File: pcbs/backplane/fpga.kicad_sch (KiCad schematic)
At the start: 77 parts, among them J2 Conn_02x15_Odd_Even, J3 Conn_02x20_Odd_Even, Q10 MMBT3906, Q11 MMBT3906, Q9 D44H11G, U10 74LVC2T45, U28 Snickerdoodle, U34 ICS501, U4 PCA9544APW, U5 PCA9544APW, U6 74HC151, U7 AP7361C-25E, U8 74LVC2T45, U9 74LVC2T45

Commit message: Backplane comms updates, manufacturing renaming
Removed misspelled "maunfacturing" folder, fixed gitignore rule to remove manufacturing folders within individual PCB folders too
Changed SCKI/SCKO terminology to SCK, SCK_LB (loopback) for clarity
Added ADC_CS loopback signal between amp ctrl board & backplane for better fast-clock timing (#38)
Backplane: changed LVDS FPGA outputs to single-ended FPGA outputs to gain more I/O pins, added external LVDS transceivers (#38)
Backplane: replaced global clock & ~LDAC buffers with a separate FPGA pin for each amp ctrl board (#38)
Backplane: removed +2.5V power supply and level translations, no longer needed without FPGA I/O pins using LVDS_25 I/O configuration
Backplane: replaced +VDC-input resistor with solder jumper (on by default)
Backplane: changed field names (Part Number to MPN) to match Aisler's naming convention for automatic recognition
Amp ctrl: fixed optional level-shifter circuit on each channel for voltage inputs (#9) schematic & channel-1 layout
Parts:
- removed C25, C27: 1uF 50V X7R, Capacitor_SMD:C_0805_2012Metric, symbol Device:C
- removed C29, C30: 100nF 50V X7R, Capacitor_SMD:C_0603_1608Metric, symbol Device:C
- removed JP34: Jumper_NC_Small, Jumper:SolderJumper-2_P1.3mm_Bridged_RoundedPad1.0x1.5mm, symbol backplane-rescue:Jumper_NC_Small-Device
- removed TP53, TP62: TestPoint, TestPoint:TestPoint_Pad_D2.0mm, symbol Connector:TestPoint
- removed TP7: TestPoint_Flag, TestPoint:TestPoint_Keystone_5019_Miniature, symbol Connector:TestPoint_Flag
- removed U7: AP7361C-25E, Package_TO_SOT_SMD:SOT-223-3_TabPin2, symbol Regulator_Linear:LT1129-3.3_SOT223
- removed U9: 74LVC2T45, Package_SO:VSSOP-8_2.3x2mm_P0.5mm, symbol Logic_LevelTranslator:74LVC2T45DC
- C21, C35: MPN (none) -> C0805C105K3RACTU; Part Number C0805C105K3RACTU -> (none)
- C22, C23, C24, C26, C28, C32, C33, C67: MPN (none) -> C0603C104K5RACTU; Part Number C0603C104K5RACTU -> (none)
- D17: MPN (none) -> UDZVTE-1716B; MPN Alt. (none) -> MM3Z16VB; Part Number UDZVTE-1716B -> (none); Part Number Alt. MM3Z16VB -> (none)
- J2: MPN (none) -> TFM-115-01-S-D-WT; MPN Alt. (none) -> TFM-115-01-L-D-WT, TFM-115-01-F-D-WT; Part Number TFM-115-01-S-D-WT -> (none); Part Number Alt. TFM-115-01-L-D-WT, TFM-115-01-F-D-WT -> (none)
- J3, JA1, JA2, JB1, JB2, JC1: MPN (none) -> TFM-120-01-S-D-WT; MPN Alt. (none) -> TFM-120-01-L-D-WT, TFM-120-01-F-D-WT; Part Number TFM-120-01-S-D-WT -> (none); Part Number Alt. TFM-120-01-L-D-WT, TFM-120-01-F-D-WT -> (none)
- Q10, Q11: MPN (none) -> MMBT3906-7-F; MPN Alt. (none) -> MMBT3906,215; Part Number MMBT3906-7-F -> (none); Part Number Alt. MMBT3906,215 -> (none)
- Q9: MPN (none) -> D44H11G; Part Number D44H11G -> (none)
- R14, R15: MPN (none) -> RK73H2ATTD4701F; Part Number RK73H2ATTD4701F -> (none)
- R73: MPN (none) -> RK73Z2ATTD; Part Number RK73Z2ATTD -> (none)
- R74: MPN (none) -> RK73H2ATTD2002F; Part Number RK73H2ATTD2002F -> (none)
- R75: MPN (none) -> RK73H2ATTD56R0F; Part Number RK73H2ATTD56R0F -> (none)
- R76: MPN (none) -> RK73H2ATTD1001F; Part Number RK73H2ATTD1001F -> (none)
- RN1, RN2: MPN (none) -> 745C101472JP; Part Number 745C101472JP -> (none)
- TP4, TP50, TP51, TP6, TP8, TP9: MPN (none) -> 5019; Part Number 5019 -> (none)
- U10, U8: MPN (none) -> 74LVC2T45DC,125; MPN Alt. (none) -> SN74LVC2T45DCUR, SN74LVC2T45DCUT; Part Number 74LVC2T45DC,125 -> (none); Part Number Alt. SN74LVC2T45DCUR, SN74LVC2T45DCUT -> (none)
- U28: MPN (none) -> 15081800/04; Part Number 15081800/04 -> (none)
- U34: MPN (none) -> 501MLFT; MPN Alt. (none) -> 501MILFT; Part Number 501MLFT -> (none); Part Number Alt. 501MILFT -> (none)
- U4, U5: MPN (none) -> PCA9544APW,118; MPN Alt. (none) -> PCA9544APWR, TCA9544APWR; Part Number PCA9544APW,118 -> (none); Part Number Alt. PCA9544APWR, TCA9544APWR -> (none)
- U6: MPN (none) -> 74HC151PW,118; MPN Alt. (none) -> SN74HC151PW; Part Number 74HC151PW,118 -> (none); Part Number Alt. SN74HC151PW -> (none)
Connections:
- net +2.5V is gone; now on net +3V3: C24.1, JA1.3 (Pin_3), JA2.3 (Pin_3), JB1.3 (Pin_3), JB2.3 (Pin_3), JC1.3 (Pin_3), U6.16 (VCC)
- net ADC_MOSI-5 is gone; now on net Power_Enable_Ext_Sense: JA1.19 (Pin_19)
- net Scanner_Clk_2.5 is gone; now on net Scanner_Clk: JB2.38 (Pin_38)
- net Trigger_2.5 is gone; now on net Trigger: JB2.36 (Pin_36)
- net Power_Enable_Ext_Sense: no longer JA1.25 (Pin_25)
- net Scanner_Clk: now reaches TP12.1, U34.5 (Clk)
- net ADC_MISO+0 renamed ~{ADC_CS_LB0}
- net ADC_MISO+1 renamed ~{ADC_CS_LB1}
- net ADC_MISO+2 renamed DAC_MISO4
- net ADC_MISO+3: no longer names the net of JB1.26 (Pin_26)
- net ADC_MISO+4 renamed ~{LDAC4}
- net ADC_MISO+5 renamed ADC_MISO5
- net ADC_MISO+6 renamed ADC_MOSI7
- net ADC_MISO+7: no longer names the net of JA1.35 (Pin_35)
- net ADC_MISO-0: no longer names the net of JB2.13 (Pin_13)
- net ADC_MISO-1 renamed ADC_MISO1
- net ADC_MISO-2 renamed ~{LDAC2}
- net ADC_MISO-3: no longer names the net of JB1.24 (Pin_24)
- net ADC_MISO-4 renamed DAC_MOSI4
- net ADC_MISO-5 renamed ~{ADC_CS_LB5}
- net ADC_MISO-6 renamed ~{ADC_CS_LB7}
- net ADC_MISO-7 renamed SCK_LB5
- net ADC_MOSI+0 renamed DAC_MOSI0
- net ADC_MOSI+1 renamed ~{DAC_CS3}
- net ADC_MOSI+2 renamed SCK2
- net ADC_MOSI+3: no longer names the net of JB2.29 (Pin_29)
- net ADC_MOSI+4 renamed SCK_LB2
- net ADC_MOSI+5 renamed ~{DAC_CS5}
- net ADC_MOSI+6 renamed ~{ADC_CS6}
- net ADC_MOSI+7: no longer names the net of JA2.32 (Pin_32)
- net ADC_MOSI-0 renamed ~{LDAC0}
- net ADC_MOSI-1 renamed ~{LDAC3}
- net ADC_MOSI-2 renamed ~{DAC_CS2}
- net ADC_MOSI-3: no longer names the net of JB2.31 (Pin_31)
- net ADC_MOSI-4 renamed ADC_MOSI2
- net ADC_MOSI-6 renamed ADC_MISO6
- net ADC_MOSI-7 renamed ~{DAC_CS6}
- net DAC_MISO+0 renamed ~{ADC_CS0}
- net DAC_MISO+1 renamed SCK1
- net DAC_MISO+2 renamed ADC_MISO2
- net DAC_MISO+3 renamed ~{ADC_CS3}
- net DAC_MISO+4 renamed ~{DAC_CS4}
- net DAC_MISO+5 renamed DAC_MOSI5
- net DAC_MISO+6 renamed DAC_MOSI6
- net DAC_MISO+7 renamed DAC_MOSI7
- net DAC_MISO-0 renamed ADC_MOSI0
- net DAC_MISO-1 renamed SCK3
- net DAC_MISO-2 renamed DAC_MISO2
- net DAC_MISO-3 renamed DAC_MISO3
- net DAC_MISO-4 renamed SCK4
- net DAC_MISO-5 renamed ~{LDAC5}
- net DAC_MISO-6 renamed ADC_MOSI6
- net DAC_MISO-7 renamed ~{LDAC7}
- net DAC_MOSI+0 renamed SCK0
- net DAC_MOSI+1 renamed ADC_MOSI1
- net DAC_MOSI+2 renamed ~{ADC_CS2}
- net DAC_MOSI+3 renamed DAC_MOSI3
- net DAC_MOSI+4 renamed ~{ADC_CS_LB6}
- net DAC_MOSI+5 renamed ~{ADC_CS5}
- net DAC_MOSI+6 renamed SCK6
- net DAC_MOSI+7 renamed ~{ADC_CS7}
- net DAC_MOSI-0 renamed ~{DAC_CS0}
- net DAC_MOSI-1 renamed ~{DAC_CS1}
- net DAC_MOSI-2 renamed ~{ADC_CS_LB2}
- net DAC_MOSI-3 renamed ADC_MOSI3
- net DAC_MOSI-4 renamed DAC_MISO6
- net DAC_MOSI-5 renamed ADC_MOSI5
- net DAC_MOSI-6 renamed ~{LDAC6}
- net DAC_MOSI-7 renamed ADC_MISO7
- net LDAC+: no longer names the net of JB2.26 (Pin_26)
- net LDAC-: no longer names the net of JB2.24 (Pin_24)
- net SCKO+0 renamed SCK_LB0
- net SCKO+1 renamed SCK_LB1
- net SCKO+2 renamed DAC_MOSI2
- net SCKO+3 renamed SCK_LB3
- net SCKO+4: no longer names the net of JC1.35 (Pin_35)
- net SCKO+5: no longer names the net of JA1.38 (Pin_38)
- net SCKO+6: no longer names the net of JA2.38 (Pin_38)
- net SCKO+7 renamed SCK_LB7
- net SCKO-0: no longer names the net of JB2.37 (Pin_37)
- net SCKO-1 renamed ADC_MISO3
- net SCKO-2 renamed SCK_LB4
- net SCKO-3: no longer names the net of JB1.37 (Pin_37)
- net SCKO-4: no longer names the net of JC1.37 (Pin_37)
- net SCKO-5 renamed DAC_MISO7
- net SCKO-6 renamed SCK_LB6
- net SCKO-7: no longer names the net of JA2.37 (Pin_37)
- net ~{ADC_CS+0}: no longer names the net of JB2.17 (Pin_17)
- net ~{ADC_CS+1} renamed DAC_MISO1
- net ~{ADC_CS+2}: no longer names the net of JC1.29 (Pin_29)
- net ~{ADC_CS+3}: no longer names the net of JB2.32 (Pin_32)
- net ~{ADC_CS+4} renamed ADC_MOSI4
- net ~{ADC_CS+5} renamed ~{DAC_CS7}
- net ~{ADC_CS+6}: no longer names the net of JA2.5 (Pin_5)
- net ~{ADC_CS+7}: no longer names the net of JA2.17 (Pin_17)
- net ~{ADC_CS-0}: no longer names the net of JB2.19 (Pin_19)
- net ~{ADC_CS-1} renamed ~{ADC_CS1}
- net ~{ADC_CS-2}: no longer names the net of JC1.31 (Pin_31)
- net ~{ADC_CS-3}: no longer names the net of JB2.30 (Pin_30)
- net ~{ADC_CS-4} renamed ~{ADC_CS4}
- net ~{ADC_CS-5} renamed SCK7
- net ~{ADC_CS-6}: no longer names the net of JA2.7 (Pin_7)
- net ~{ADC_CS-7}: no longer names the net of JA2.19 (Pin_19)
- net ~{DAC_CS+0} renamed DAC_MISO0
- net ~{DAC_CS+1} renamed ~{LDAC1}
- net ~{DAC_CS+2} renamed ADC_MISO4
- net ~{DAC_CS+3} renamed ~{ADC_CS_LB3}
- net ~{DAC_CS+4}: no longer names the net of JA2.11 (Pin_11)
- net ~{DAC_CS+5}: no longer names the net of JA1.20 (Pin_20)
- net ~{DAC_CS+6}: no longer names the net of JA2.23 (Pin_23)
- net ~{DAC_CS+7} renamed SCK5
- net ~{DAC_CS-0} renamed ADC_MISO0
- net ~{DAC_CS-1} renamed DAC_MOSI1
- net ~{DAC_CS-2} renamed ~{ADC_CS_LB4}
- net ~{DAC_CS-3}: no longer names the net of JB1.30 (Pin_30)
- net ~{DAC_CS-4}: no longer names the net of JA2.13 (Pin_13)
- net ~{DAC_CS-5} renamed DAC_MISO5
- net ~{DAC_CS-6}: no longer names the net of JA2.25 (Pin_25)
- net ~{DAC_CS-7}: no longer names the net of JA1.31 (Pin_31)
- net ~{SCKI+}: no longer names the net of JB2.23 (Pin_23)
- net ~{SCKI-}: no longer names the net of JB2.25 (Pin_25)
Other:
- removed sheet Clock Fanout Buffer
- removed sheet LDAC Fanout Buffer
- note added: "+1.8V logic"
- note added: "I/O bank 13"
- note added: "I/O bank 34"
- note added: "I/O bank 35"
- note added: "Pinout chosen only for easy routing, except... * SCK_LB signals must be on SRCC/MRCC pins (35/37 or 36/38 on JA*-JC*, or 5/7, 6/8 on JC1) * Scanner_Clk signal must be on MRCC pin (36/38 on JA*-JC*, or 6/8 on JC1)"
- note added: "Snickerdoodle Black has all MIO pins (CPU peripherals) powered from +1.8V, so need to supply the I2C mux with +1.8V to block higher voltages (3.3V logic on amp boards) from reaching the MIO pins"
- note removed: "2.5V logic"
- note removed: "Channels arranged out-of-order (no functional difference) for easy routing"
- note removed: "Pinout chosen only for easy routing, except... * SCKO signals must be on SRCC/MRCC pins (35/37 or 36/38 on JA*-JC*, or 5/7, 6/8 on JC1) * 10 Mhz signal must be on MRCC pin (36/38 on JA*-JC*, or 6/8 on JC1)"
- note removed: "Requirements: 600 mA Iout-max Dropout voltage < 0.8V @ 600 mA"
- note removed: "Snickerdoodle Black has all MIO pins (CPU peripherals) powered from +1.8V, so need to supply the I2C mux with 1.8V to block higher voltages (3.3V logic on amp boards) from reaching the MIO pins"

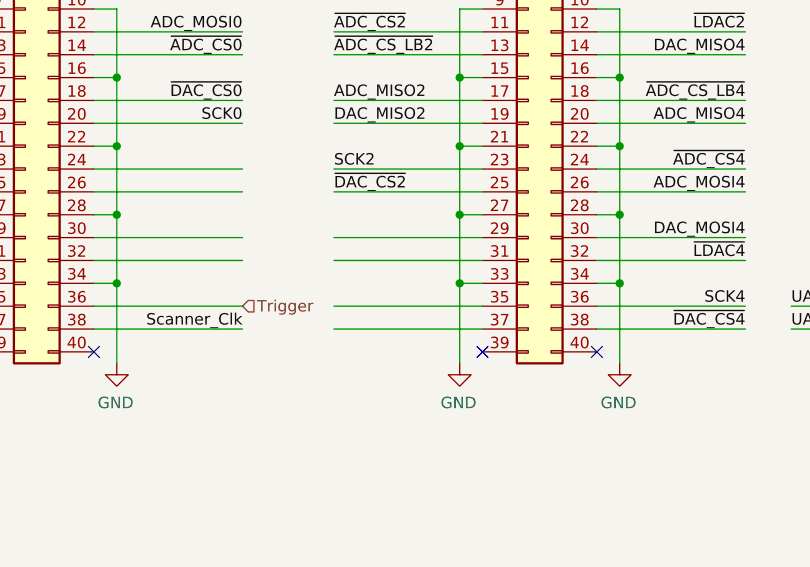
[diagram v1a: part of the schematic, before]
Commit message: Optical Ethernet, closed-loop response prediction
Backplane: added optical Ethernet interface with transceiver AFBR-5972Z, updated pinout (fixes #44)
Backplane: cleaned up schematic readability slightly (assigned sheet background colors)
Docs: added closed-loop response plotting to compensation script
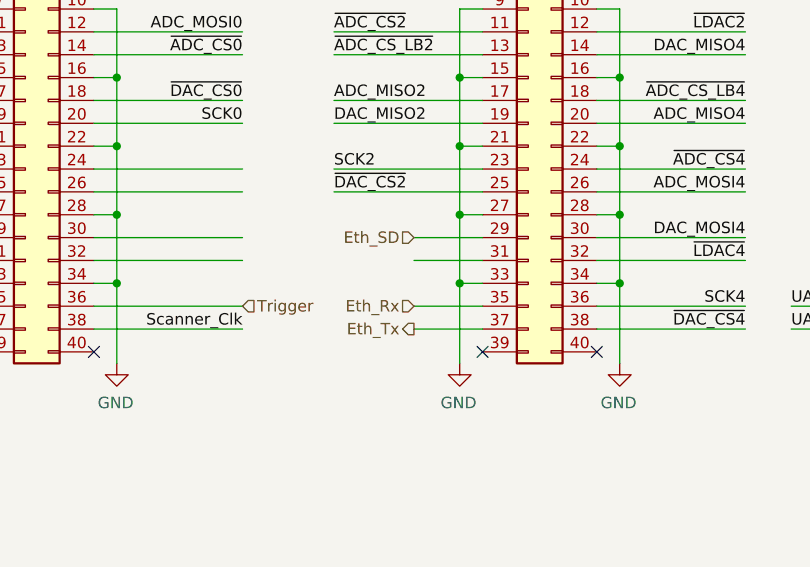
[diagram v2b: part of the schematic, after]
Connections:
- net Eth_SD: now reaches JC1.29 (Pin_29)
- net Eth_Rx: now reaches JC1.35 (Pin_35)
- net Eth_Tx: now reaches JC1.37 (Pin_37)
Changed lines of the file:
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@@
 	(wire
 		(pts
+			(xy 264.16 78.74) (xy 271.78 78.74)
+		)
+		(stroke
+			(width 0)
+			(type default)
+		)
+	)
+	(wire
+		(pts
 			(xy 71.12 149.86) (xy 80.01 149.86)
 		)
@@
 	(wire
 		(pts
-			(xy 271.78 68.58) (xy 255.27 68.58)
+			(xy 271.78 68.58) (xy 264.16 68.58)
 		)
 		(stroke
@@
 	(wire
 		(pts
-			(xy 271.78 71.12) (xy 255.27 71.12)
+			(xy 271.78 71.12) (xy 264.16 71.12)
 		)
 		(stroke
@@
 	(wire
 		(pts
-			(xy 271.78 78.74) (xy 255.27 78.74)
-		)
-		(stroke
-			(width 0)
-			(type default)
-		)
-	)
-	(wire
-		(pts
 			(xy 156.21 34.29) (xy 156.21 35.56)
 		)
@@
 	(wire
 		(pts
-			(xy 271.78 76.2) (xy 255.27 76.2)
-		)
-		(stroke
-			(width 0)
-			(type default)
-		)
-	)
-	(wire
-		(pts
 			(xy 116.84 50.8) (xy 119.38 50.8)
 		)
@@
 	(wire
 		(pts
+			(xy 264.16 76.2) (xy 271.78 76.2)
+		)
+		(stroke
+			(width 0)
+			(type default)
+		)
+	)
+	(wire
+		(pts
 			(xy 160.02 48.26) (xy 143.51 48.26)
 		)
@@
 		)
 	)
+	(hierarchical_label "Eth_Tx"
+		(shape output)
+		(at 264.16 78.74 180)
+		(effects
+			(font
+				(size 1.27 1.27)
+			)
+			(justify right)
+		)
+	)
 	(hierarchical_label "SCK[0..7]"
 		(shape output)
@@
 		)
 	)
+	(hierarchical_label "Eth_Rx"
+		(shape input)
+		(at 264.16 76.2 180)
+		(effects
+			(font
+				(size 1.27 1.27)
+			)
+			(justify right)
+		)
+	)
+	(hierarchical_label "Eth_SD"
+		(shape input)
+		(at 264.16 68.58 180)
+		(effects
+			(font
+				(size 1.27 1.27)
+			)
+			(justify right)
+		)
+	)

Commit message: Added dedicated Ethernet PHY IC to backplane
Backplane: added DP83822 PHY IC, instead of relying on FPGA's PL for PHY logic (fixes #44)
Libraries: added DP83822 symbol & footprint
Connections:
- net Eth_SD: now also J3.30 (Pin_30); no longer JC1.29 (Pin_29)
- net RGMII_TX_D3: now reaches J3.11 (Pin_11)
- net RGMII_RX_D0: now reaches J3.12 (Pin_12)
- net RGMII_TX_CTL: now reaches J3.13 (Pin_13)
- net RGMII_RX_CLK: now reaches J3.14 (Pin_14)
- net RGMII_RX_D1: now reaches J3.17 (Pin_17)
- net RGMII_RX_CTL: now reaches J3.18 (Pin_18)
- net RGMII_RX_D2: now reaches J3.19 (Pin_19)
- net MDC: now reaches J3.2 (Pin_2)
- net RGMII_RX_D3: now reaches J3.20 (Pin_20)
- net ~{ETH_RESET}: now reaches J3.24 (Pin_24)
- net ~{ETH_OSC_PWDN}: now reaches J3.26 (Pin_26)
- net ~{ETH_PWDN}: now reaches J3.32 (Pin_32)
- net MDIO: now reaches J3.4 (Pin_4)
- net RGMII_TX_CLK: now reaches J3.5 (Pin_5)
- net RGMII_TX_D2: now reaches J3.6 (Pin_6)
- net RGMII_TX_D0: now reaches J3.7 (Pin_7)
- net RGMII_TX_D1: now reaches J3.8 (Pin_8)
- net Eth_Rx: no longer names the net of JC1.35 (Pin_35)
- net Eth_Tx: no longer names the net of JC1.37 (Pin_37)
- no-connect marks 68 -> 50
